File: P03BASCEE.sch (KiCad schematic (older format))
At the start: 13 parts, among them U1 24LC1025, U2 24LC1025, U3 DS13375+, U4 ATMEGA328P-AU, Y1 Crystal 32MHz, Y2 Crystal 16MHz

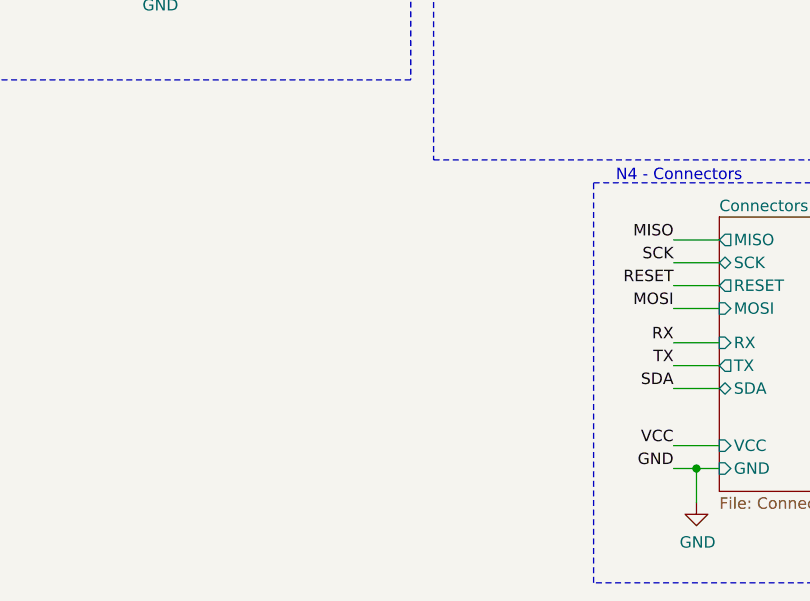
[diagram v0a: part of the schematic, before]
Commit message: Furos de parafuso adicionados no esquemático e no PCB (boa prática)
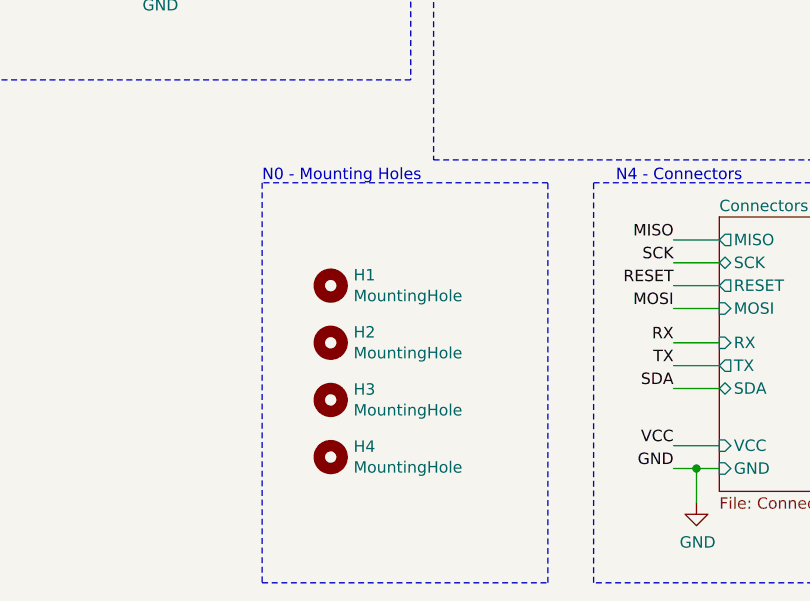
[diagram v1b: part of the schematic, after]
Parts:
- added H1, H2, H3, H4: MountingHole, MountingHole:MountingHole_3mm, symbol Mechanical:MountingHole
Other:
- note added: "N0 - Mounting Holes"
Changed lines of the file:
@@
 	1400 3650 4150 3650
-Wire Notes Line
-	4950 5850 6750 5850
 Wire Notes Line
 	6750 5850 6750 7600
@@
 Text Notes 5600 5850 2    50   ~ 0
 N4 - Connectors
+$Comp
+L Mechanical:MountingHole H1
+U 1 1 5F1118A8
+P 3800 6300
+F 0 "H1" H 3900 6346 50  0000 L CNN
+F 1 "MountingHole" H 3900 6255 50  0000 L CNN
+F 2 "MountingHole:MountingHole_3mm" H 3800 6300 50  0001 C CNN
+F 3 "~" H 3800 6300 50  0001 C CNN
+	1    3800 6300
+	1    0    0    -1
+$EndComp
+$Comp
+L Mechanical:MountingHole H2
+U 1 1 5F111EAB
+P 3800 6550
+F 0 "H2" H 3900 6596 50  0000 L CNN
+F 1 "MountingHole" H 3900 6505 50  0000 L CNN
+F 2 "MountingHole:MountingHole_3mm" H 3800 6550 50  0001 C CNN
+F 3 "~" H 3800 6550 50  0001 C CNN
+	1    3800 6550
+	1    0    0    -1
+$EndComp
+$Comp
+L Mechanical:MountingHole H3
+U 1 1 5F11244C
+P 3800 6800
+F 0 "H3" H 3900 6846 50  0000 L CNN
+F 1 "MountingHole" H 3900 6755 50  0000 L CNN
+F 2 "MountingHole:MountingHole_3mm" H 3800 6800 50  0001 C CNN
+F 3 "~" H 3800 6800 50  0001 C CNN
+	1    3800 6800
+	1    0    0    -1
+$EndComp
+$Comp
+L Mechanical:MountingHole H4
+U 1 1 5F11266E
+P 3800 7050
+F 0 "H4" H 3900 7096 50  0000 L CNN
+F 1 "MountingHole" H 3900 7005 50  0000 L CNN
+F 2 "MountingHole:MountingHole_3mm" H 3800 7050 50  0001 C CNN
+F 3 "~" H 3800 7050 50  0001 C CNN
+	1    3800 7050
+	1    0    0    -1
+$EndComp
+Wire Notes Line
+	4950 5850 6750 5850
+Wire Notes Line
+	3500 7600 4750 7600
+Wire Notes Line
+	4750 7600 4750 5850
+Wire Notes Line
+	4750 5850 3500 5850
+Wire Notes Line
+	3500 5850 3500 7600
+Text Notes 3500 5850 0    50   ~ 0
+N0 - Mounting Holes
 $EndSCHEMATC

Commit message: Criada borda da placa - buracos de montagem reduzidos para 2.2mm e incluídos
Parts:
- H1, H2, H3, H4: footprint MountingHole:MountingHole_3mm -> MountingHole:MountingHole_2.2mm_M2_DIN965
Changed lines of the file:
@@
 F 0 "H1" H 3900 6346 50  0000 L CNN
 F 1 "MountingHole" H 3900 6255 50  0000 L CNN
-F 2 "MountingHole:MountingHole_3mm" H 3800 6300 50  0001 C CNN
+F 2 "MountingHole:MountingHole_2.2mm_M2_DIN965" H 3800 6300 50  0001 C CNN
 F 3 "~" H 3800 6300 50  0001 C CNN
 	1    3800 6300
@@
 F 0 "H2" H 3900 6596 50  0000 L CNN
 F 1 "MountingHole" H 3900 6505 50  0000 L CNN
-F 2 "MountingHole:MountingHole_3mm" H 3800 6550 50  0001 C CNN
+F 2 "MountingHole:MountingHole_2.2mm_M2_DIN965" H 3800 6550 50  0001 C CNN
 F 3 "~" H 3800 6550 50  0001 C CNN
 	1    3800 6550
@@
 F 0 "H3" H 3900 6846 50  0000 L CNN
 F 1 "MountingHole" H 3900 6755 50  0000 L CNN
-F 2 "MountingHole:MountingHole_3mm" H 3800 6800 50  0001 C CNN
+F 2 "MountingHole:MountingHole_2.2mm_M2_DIN965" H 3800 6800 50  0001 C CNN
 F 3 "~" H 3800 6800 50  0001 C CNN
 	1    3800 6800
@@
 F 0 "H4" H 3900 7096 50  0000 L CNN
 F 1 "MountingHole" H 3900 7005 50  0000 L CNN
-F 2 "MountingHole:MountingHole_3mm" H 3800 7050 50  0001 C CNN
+F 2 "MountingHole:MountingHole_2.2mm_M2_DIN965" H 3800 7050 50  0001 C CNN
 F 3 "~" H 3800 7050 50  0001 C CNN
 	1    3800 7050
